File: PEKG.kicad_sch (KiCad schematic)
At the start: 107 parts, among them J1 AudioJack4, J2 AudioJack3, U1 TL072, U12 NCS21802DMR2G, U13 NCS21802DMR2G, U2 TL072, U3 INA350CDSIDDFR, U7 TLV61070ADBVR, U8 NCS21802DMR2G

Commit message: dfs
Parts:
- BT1: footprint Battery:BatteryHolder_Keystone_2462_2xAA -> PEKG:battery_holder
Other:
- note added: "MOŽDA DODATI POTENCIOMETAR"
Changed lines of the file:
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@@
 	(text "DOUBLE CHECK VREDNOSTI"
 		(exclude_from_sim no)
-		(at 251.968 337.566 0)
+		(at 229.87 263.144 0)
 		(effects
 			(font
@@
 	(text "PRERAČUNATI PROPUSNE OPSEGE"
 		(exclude_from_sim no)
-		(at 255.778 329.692 0)
+		(at 233.68 255.27 0)
 		(effects
 			(font
@@
 		)
 	)
+	(text "MOŽDA DODATI POTENCIOMETAR"
+		(exclude_from_sim no)
+		(at 92.456 259.334 0)
+		(effects
+			(font
+				(size 5.08 5.08)
+				(color 255 0 0 1)
+			)
+		)
+	)
 	(text_box "Input voltage range: 10 uV - 5 mV"
 		(exclude_from_sim no)
@@
 			)
 		)
-		(property "Footprint" "Battery:BatteryHolder_Keystone_2462_2xAA"
+		(property "Footprint" "PEKG:battery_holder"
 			(at 21.59 195.326 90)
 			(effects

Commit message: Schematic done.
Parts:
- removed C48: 10u, Resistor_SMD:R_1206_3216Metric_Pad1.30x1.75mm_HandSolder, symbol Device:C
- removed J2: AudioJack3, PEKG:Jack_3.5mm_CUI_SJ1-3523N_Horizontal, symbol Connector_Audio:AudioJack3
- removed L2: 4.7u, Inductor_THT:L_Radial_D7.5mm_P3.50mm_Fastron_07P, symbol Device:L
- removed TP10: TestPoint, TestPoint:TestPoint_Pad_D3.0mm, symbol Connector:TestPoint
- removed U1, U2: TL072, Package_SO:SOIC-8_3.9x4.9mm_P1.27mm, symbol Amplifier_Operational:TL072
- added J2: AudioJack3_SwitchTR, PEKG:Jack_3.5mm_CUI_SJ1-3525N_Horizontal, symbol Connector_Audio:AudioJack3_SwitchTR
- added JP10: Jumper_2_Open, Jumper:SolderJumper-2_P1.3mm_Open_RoundedPad1.0x1.5mm, symbol Jumper:Jumper_2_Open
- added JP9: Jumper_2_Bridged, Jumper:SolderJumper-2_P1.3mm_Bridged_RoundedPad1.0x1.5mm, symbol Jumper:Jumper_2_Bridged
- added R12: 10k, Resistor_SMD:R_0603_1608Metric_Pad0.98x0.95mm_HandSolder, symbol Device:R
- added R2: 100, Resistor_SMD:R_0603_1608Metric_Pad0.98x0.95mm_HandSolder, symbol Device:R
- added U1, U2: TLV9062, Package_SO:SOIC-8_3.9x4.9mm_P1.27mm, symbol Amplifier_Operational:TLV9062
- J1: footprint Connector_Audio:Jack_3.5mm_CUI_SJ1-3524N_Horizontal -> PEKG:Jack_3.5mm_4pole; Kelco (none) -> https://www.tme.eu/Document/8cf9d7ee9160c565a011641a9306e3c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
- U7: footprint Package_TO_SOT_SMD:SOT-23-6 -> Package_TO_SOT_SMD:SOT-23-6_Handsoldering
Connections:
- net Earth is gone; now on net GND: C22.1, C41.1, C47.1, R63.1, U7.2 (GND)
- net FIL_OUT: now also U2.1
- net GAIN_500_OUTPUT: now also JP10.2 (B), JP9.2 (B), U1.3 (+); no longer C15.1, C21.1, R29.2, R57.2, R61.2, TP4.1, U12.1
- net GAIN_50_OUTPUT: now also U1.5 (+)
- net GND: now also R12.1, U1.4 (V-), U2.4 (V-)
- net LEFT_ARM: now also J2.R
- net LEVELED_OUTPUT: now also R2.2; no longer J1.R2
- net RIGHT_ARM: now also J2.S
- net RIGHT_LEG_DRIVE: now also J2.T
- net at C21.2, R35.2, R57.1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: now also U1.6 (-)
- net SW: now reaches L3.2, U7.1 (SW)
- net at C24.1, JP5.1 (A), R27.2: now also U2.7
- net at C16.2, R26.2, R51.1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: now also U1.2 (-)
- net at C16.1, JP4.1 (A), R51.2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: now also U1.1
- net SW_OUT: now reaches C22.2, C41.2, JP8.1 (A), R62.2, U7.5 (VOUT)
- net FB: now reaches R62.1, R63.2, U7.4 (FB)
- net at C24.2, R27.1, R47.2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: now also U2.6 (-)
- net at R30.2, R31.2: now also U2.5 (+)
- net at C18.1, R34.1, R38.1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: now also U2.2 (-)
- net 2.5V renamed V_{ref}
- net V_{ref}: now also U2.3 (+)
- net VBUS renamed V_{cc}
- net V_{cc}: now also U1.8 (V+), U2.8 (V+)
- new net: C21.1, JP10.1 (A), R57.2, R61.2, U1.7
- new net: C15.1, JP9.1 (A), R29.2, TP4.1, U12.1
- new net: J1.R2, R12.2, R2.1
- no-connect marks 3 -> 5
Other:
- note added: "https://www.tme.eu/rs/en/details/jc-128/jack-connectors/changzhou-dahua-imp-and-exp-group-co/vg01218/"
- moved on the sheet: BT1, C13, C15, C19, C20, C21, C22, C26, C44, C46, C47, H1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

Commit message: Updated leg drive, output connector, boost converter.
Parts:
- added C25: 10n, Capacitor_SMD:C_0603_1608Metric_Pad1.08x0.95mm_HandSolder, symbol Device:C
- added C48: 10u, Capacitor_SMD:C_0603_1608Metric_Pad1.08x0.95mm_HandSolder, symbol Device:C
- added TP10, TP12, TP13, TP14: TestPoint, TestPoint:TestPoint_Pad_D3.0mm, symbol Connector:TestPoint
- C22: value 1u -> 10u; footprint Resistor_SMD:R_0603_1608Metric_Pad0.98x0.95mm_HandSolder -> Capacitor_SMD:C_0603_1608Metric_Pad1.08x0.95mm_HandSolder; LCSC (none) -> C96446
- C41, C47: footprint Resistor_SMD:R_1206_3216Metric_Pad1.30x1.75mm_HandSolder -> Capacitor_SMD:C_0603_1608Metric_Pad1.08x0.95mm_HandSolder; LCSC (none) -> C96446
- R62, R63: LCSC (none) -> C25804
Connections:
- net COMMON_INPUT_LEVEL: now also C25.1
- net GND: now also J1.R2, TP13.1, TP14.1; no longer J1.S
- net LA_IN: now also TP12.1
- net RA_IN: now also TP10.1
- net at R13.1, U12.7: now also C25.2
- new net: C48.2, R2.1
- new net: C48.1, J1.S, R12.2
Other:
- note removed: "DOUBLE CHECK VREDNOSTI"
- note removed: "MOŽDA DODATI POTENCIOMETAR"
- note removed: "PRERAČUNATI PROPUSNE OPSEGE"
- note removed: "https://www.tme.eu/rs/en/details/jc-128/jack-connectors/changzhou-dahua-imp-and-exp-group-co/vg01218/"
- moved on the sheet: J1, R12, R13, R2, R46

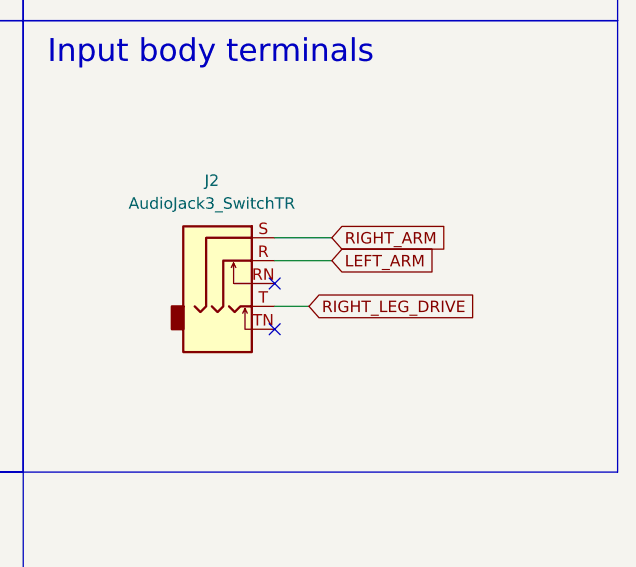
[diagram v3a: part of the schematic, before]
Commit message: Updated input conn, updated battery holder.
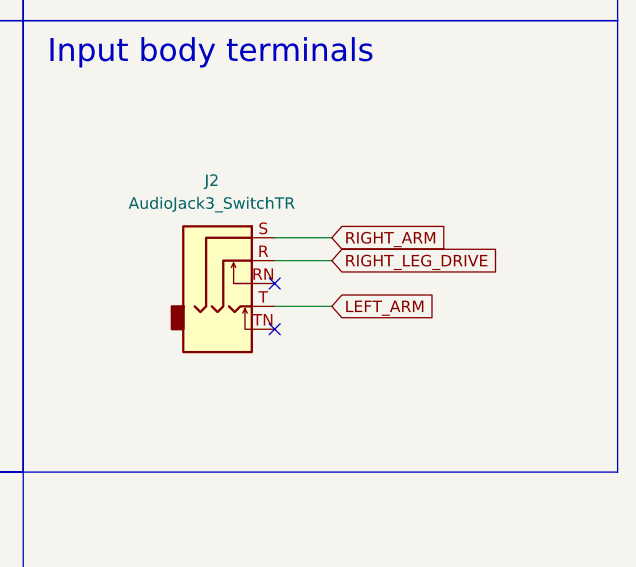
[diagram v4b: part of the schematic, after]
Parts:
- BT1: footprint PEKG:battery_holder -> PEKG:MG_battery_holder
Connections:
- net LEFT_ARM: now also J2.T; no longer J2.R
- net RIGHT_LEG_DRIVE: now also J2.R; no longer J2.T
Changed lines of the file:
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@@
 	(wire
 		(pts
-			(xy 373.38 152.4) (xy 369.57 152.4)
+			(xy 375.92 152.4) (xy 369.57 152.4)
 		)
 		(stroke
@@
 		)
 	)
+	(global_label "RIGHT_LEG_DRIVE"
+		(shape input)
+		(at 375.92 147.32 0)
+		(fields_autoplaced yes)
+		(effects
+			(font
+				(size 1.27 1.27)
+			)
+			(justify left)
+		)
+		(property "Intersheetrefs" "${INTERSHEET_REFS}"
+			(at 395.1128 147.32 0)
+			(effects
+				(font
+					(size 1.27 1.27)
+				)
+				(justify left)
+				(hide yes)
+			)
+		)
+	)
 	(global_label "V_{ref}"
 		(shape input)
@@
 		)
 	)
-	(global_label "RIGHT_LEG_DRIVE"
-		(shape input)
-		(at 373.38 152.4 0)
-		(fields_autoplaced yes)
-		(effects
-			(font
-				(size 1.27 1.27)
-			)
-			(justify left)
-		)
-		(property "Intersheetrefs" "${INTERSHEET_REFS}"
-			(at 392.5728 152.4 0)
-			(effects
-				(font
-					(size 1.27 1.27)
-				)
-				(justify left)
-				(hide yes)
-			)
-		)
-	)
 	(global_label "FIL_OUT"
 		(shape input)
@@
 		)
 	)
-	(global_label "LEFT_ARM"
-		(shape input)
-		(at 375.92 147.32 0)
-		(fields_autoplaced yes)
-		(effects
-			(font
-				(size 1.27 1.27)
-			)
-			(justify left)
-		)
-		(property "Intersheetrefs" "${INTERSHEET_REFS}"
-			(at 387.9161 147.32 0)
-			(effects
-				(font
-					(size 1.27 1.27)
-				)
-				(justify left)
-				(hide yes)
-			)
-		)
-	)
 	(global_label "V_{ref}"
 		(shape output)
@@
 		)
 	)
+	(global_label "LEFT_ARM"
+		(shape input)
+		(at 375.92 152.4 0)
+		(fields_autoplaced yes)
+		(effects
+			(font
+				(size 1.27 1.27)
+			)
+			(justify left)
+		)
+		(property "Intersheetrefs" "${INTERSHEET_REFS}"
+			(at 387.9161 152.4 0)
+			(effects
+				(font
+					(size 1.27 1.27)
+				)
+				(justify left)
+				(hide yes)
+			)
+		)
+	)
 	(global_label "RIGHT_ARM"
 		(shape input)
@@
 			)
 		)
-		(property "Footprint" "PEKG:battery_holder"
+		(property "Footprint" "PEKG:MG_battery_holder"
 			(at 22.86 204.216 90)
 			(effects

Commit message: all hail JFET.
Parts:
- added D3: LED, LED_SMD:LED_0603_1608Metric_Pad1.05x0.95mm_HandSolder, symbol Device:LED
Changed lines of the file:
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@@
+	)
+	(symbol
+		(lib_id "Device:LED")
+		(at 60.96 252.73 0)
+		(unit 1)
+		(exclude_from_sim no)
+		(in_bom yes)
+		(on_board yes)
+		(dnp no)
+		(fields_autoplaced yes)
+		(property "Reference" "D3"
+			(at 59.3725 246.38 0)
+			(effects
+				(font
+					(size 1.27 1.27)
+				)
+			)
+		)
+		(property "Value" "LED"
+			(at 59.3725 248.92 0)
+			(effects
+				(font
+					(size 1.27 1.27)
+				)
+			)
+		)
+		(property "Footprint" "LED_SMD:LED_0603_1608Metric_Pad1.05x0.95mm_HandSolder"
+			(at 60.96 252.73 0)
+			(effects
+				(font
+					(size 1.27 1.27)
+				)
+				(hide yes)
+			)
+		)
+		(property "Datasheet" "~"
+			(at 60.96 252.73 0)
+			(effects
+				(font
+					(size 1.27 1.27)
+				)
+				(hide yes)
+			)
+		)
+		(property "Description" "Light emitting diode"
+			(at 60.96 252.73 0)
+			(effects
+				(font
+					(size 1.27 1.27)
+				)
+				(hide yes)
+			)
+		)
+		(property "Sim.Pins" "1=K 2=A"
+			(at 60.96 252.73 0)
+			(effects
+				(font
+					(size 1.27 1.27)
+				)
+				(hide yes)
+			)
+		)
+		(property "JLCPCB" "C2286"
+			(at 60.96 252.73 0)
+			(effects
+				(font
+					(size 1.27 1.27)
+				)
+				(hide yes)
+			)
+		)
+		(pin "1"
+		)
+		(pin "2"
+		)
+		(instances
+			(project ""
+				(path "/6b6ace37-3aeb-4177-8f53-de4683f890d9"
+					(reference "D3")
+					(unit 1)
+				)
+			)
+		)
 	)
 	(symbol

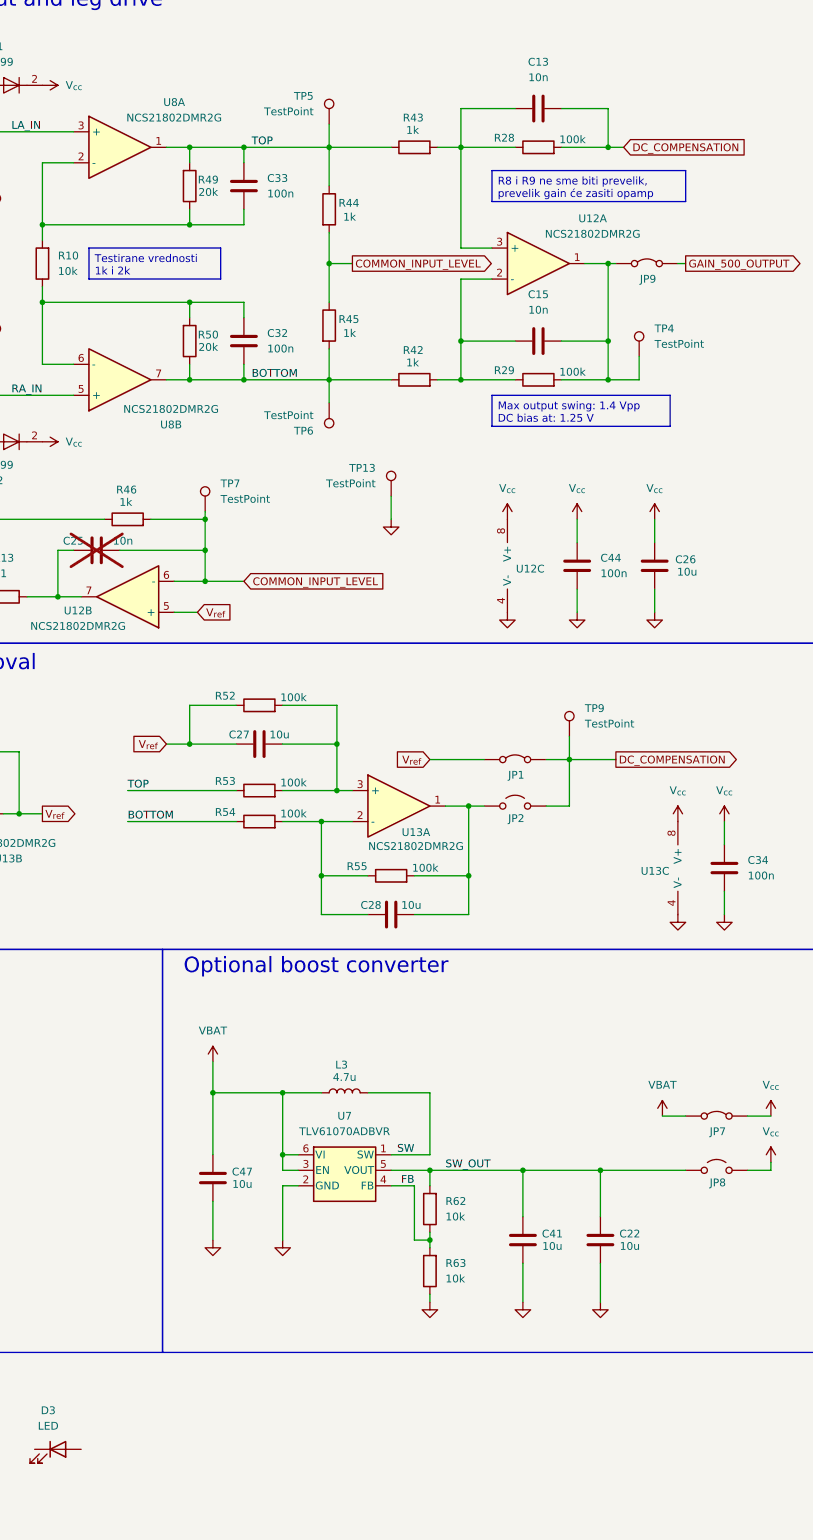
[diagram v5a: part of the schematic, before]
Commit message: Fixed inverted DC off, reduced gain from 500 to 5
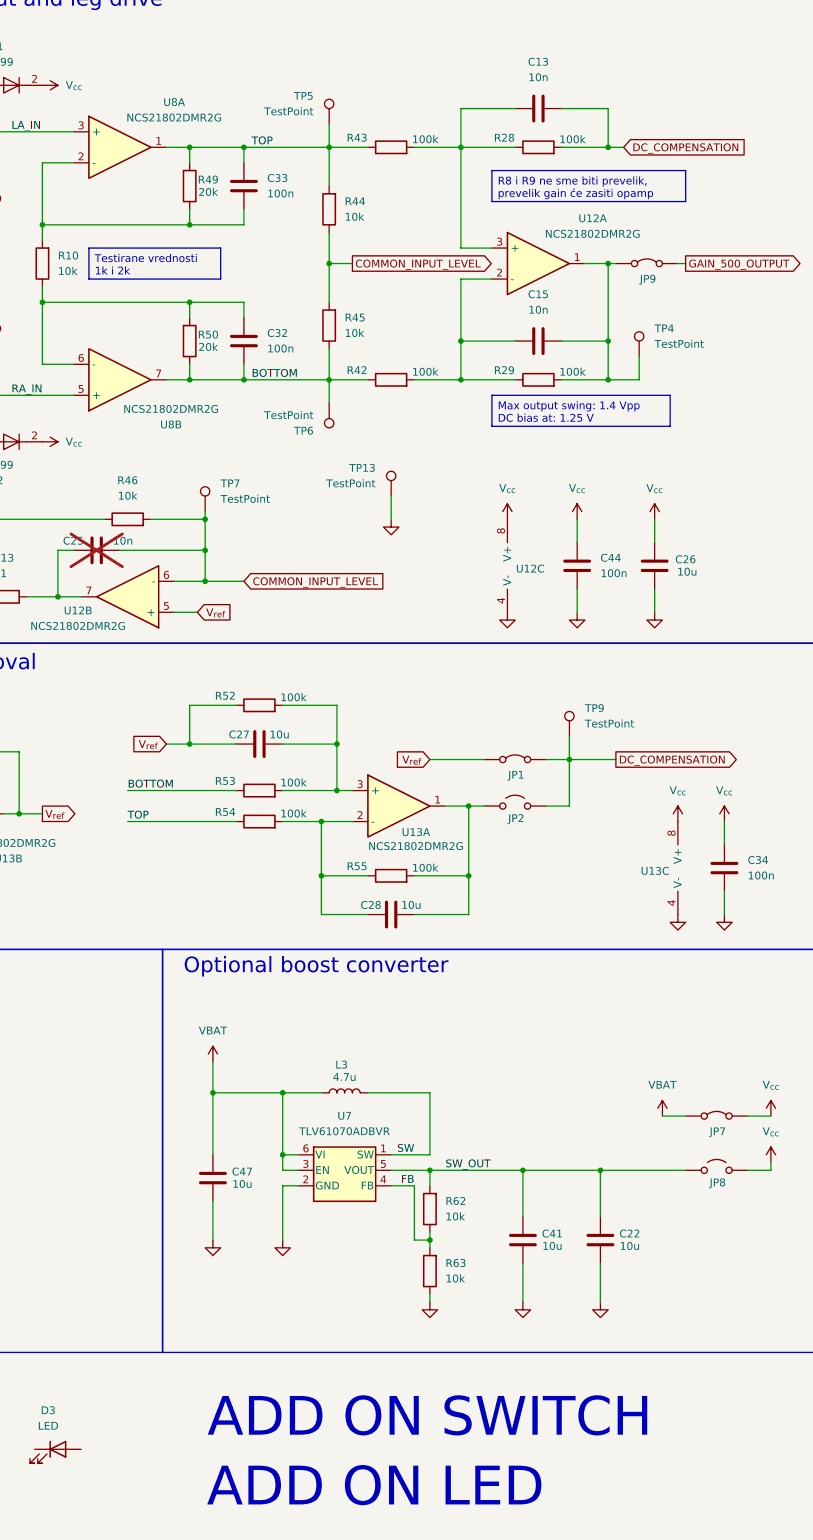
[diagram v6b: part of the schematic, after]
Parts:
- R42, R43: value 1k -> 100k; LCSC C21190 -> C25803
- R44, R45, R46: value 1k -> 10k; LCSC C21190 -> C25804
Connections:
- net BOTTOM: now also R45.1, R53.1; no longer R45.2, R54.1
- net COMMON_INPUT_LEVEL: now also R44.1, R45.2; no longer R44.2, R45.1
- net TOP: now also R44.2, R54.1; no longer R44.1, R53.1
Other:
- note added: "ADD ON LED"
- note added: "ADD ON SWITCH"

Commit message: added sw
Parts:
- removed C21: 10n, Capacitor_SMD:C_0603_1608Metric_Pad1.08x0.95mm_HandSolder, symbol Device:C
- removed C22, C41: 10u, Capacitor_SMD:C_0603_1608Metric_Pad1.08x0.95mm_HandSolder, symbol Device:C
- removed C46: 100n, Capacitor_SMD:C_0603_1608Metric_Pad1.08x0.95mm_HandSolder, symbol Device:C
- removed JP1, JP7: Jumper_2_Bridged, Jumper:SolderJumper-2_P1.3mm_Bridged_RoundedPad1.0x1.5mm, symbol Jumper:Jumper_2_Bridged
- removed JP10, JP2, JP8: Jumper_2_Open, Jumper:SolderJumper-2_P1.3mm_Open_RoundedPad1.0x1.5mm, symbol Jumper:Jumper_2_Open
- removed L3: 4.7u, Inductor_SMD:L_Bourns_SRN6045TA, symbol Device:L
- removed R23, R32, R57: 100k, Resistor_SMD:R_0603_1608Metric_Pad0.98x0.95mm_HandSolder, symbol Device:R
- removed R35, R62, R63: 10k, Resistor_SMD:R_0603_1608Metric_Pad0.98x0.95mm_HandSolder, symbol Device:R
- removed R61: 1Meg, Resistor_SMD:R_0603_1608Metric_Pad0.98x0.95mm_HandSolder, symbol Device:R
- removed TP11: TestPoint, TestPoint:TestPoint_Pad_D3.0mm, symbol Connector:TestPoint
- removed unit 2 of U1
- removed unit 1 of U1
- removed U13: NCS21802DMR2G, Package_SO:OnSemi_Micro8, symbol voltmeter_lib:NCS21802DMR2G
- removed U3: INA350CDSIDDFR, Package_SO:MSOP-8_3x3mm_P0.65mm, symbol PEKG_lib:INA350CDSIDDFR
- removed U7: TLV61070ADBVR, Package_TO_SOT_SMD:SOT-23-6_Handsoldering, symbol DS100M08KV:TLV61070ADBVR
- added SW1: SW_DPDT_x2, PEKG:DPDT_bigger, symbol Switch:SW_DPDT_x2
- added U4: TLV9062, Package_SO:SOIC-8_3.9x4.9mm_P1.27mm, symbol Amplifier_Operational:TLV9062
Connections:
- net COMMON_INPUT_LEVEL: no longer U12.6 (-)
- net DC_COMPENSATION: now also C28.2, R55.2, U4.7
- net GND: now also U4.4 (V-)
- net VBAT: now also SW1.3 (C)
- net V_{cc}: now also SW1.2 (B), U4.8 (V+)
- net V_{ref}: now also U4.1, U4.2 (-); no longer U12.5 (+)
- net at C27.2, R52.2, R53.2: now also U4.5 (+)
- net at C23.1, R18.1, R24.2: now also U4.3 (+)
- net at C16.2, R26.2, R51.1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: now also U12.6 (-)
- net at C16.1, JP4.1 (A), R51.2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: now also U12.7
- net at C25.2, R13.1: no longer U12.7
- net at C28.1, R54.2, R55.1: now also U4.6 (-)
- net GAIN_5000_OUTPUT renamed GAIN_50
- net GAIN_500_OUTPUT renamed GAIN_5
- net GAIN_5: now also U12.5 (+)
- no-connect marks 5 -> 4
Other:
- note removed: "Optional instrumentation amp"
- moved on the sheet: TP9

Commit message: opop
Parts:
- removed C24: 10n, Capacitor_SMD:C_0603_1608Metric_Pad1.08x0.95mm_HandSolder, symbol Device:C
- removed C42: 100n, Capacitor_SMD:C_0603_1608Metric_Pad1.08x0.95mm_HandSolder, symbol Device:C
- removed JP5: Jumper_2_Open, Jumper:SolderJumper-2_P1.3mm_Open_RoundedPad1.0x1.5mm, symbol Jumper:Jumper_2_Open
- removed JP6: Jumper_2_Bridged, Jumper:SolderJumper-2_P1.3mm_Bridged_RoundedPad1.0x1.5mm, symbol Jumper:Jumper_2_Bridged
- removed R27, R30, R31: 10k, Resistor_SMD:R_0603_1608Metric_Pad0.98x0.95mm_HandSolder, symbol Device:R
- removed R47, R48: 20k, Resistor_SMD:R_0603_1608Metric_Pad0.98x0.95mm_HandSolder, symbol Device:R
- removed TP1: TestPoint, TestPoint:TestPoint_Pad_D3.0mm, symbol Connector:TestPoint
- removed unit 3 of U2
- added R1: 10k, Resistor_SMD:R_0603_1608Metric_Pad0.98x0.95mm_HandSolder, symbol Device:R
- renumbered U1 to U2
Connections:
- net LEVELED_OUTPUT is gone; now on net FIL_OUT: R2.2
- net COMMON_INPUT_LEVEL: now also U2.6 (-)
- net GND: now also D3.1 (K)
- net V_{cc}: now also SW1.5 (B)
- net V_{ref}: now also U2.5 (+)
- net at U2.7: now also C25.2, R13.1
- net at D3.2 (A): now also R1.1
- net at SW1.6 (C): now also R1.2
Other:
- note removed: "Common mode change"
- moved on the sheet: C14, C43, D3, SW1B, U2B, U2C
